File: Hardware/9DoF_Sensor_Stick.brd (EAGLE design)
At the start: 25.4 x 10.2 mm, 19 parts, among them U1 LSM9DS1

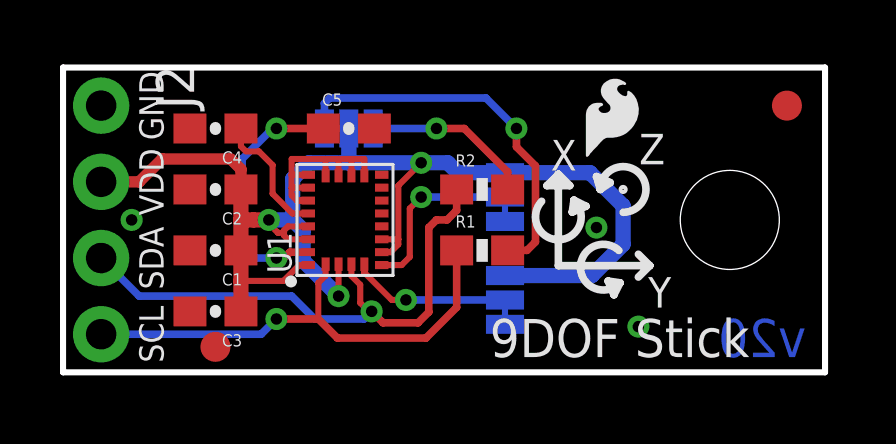
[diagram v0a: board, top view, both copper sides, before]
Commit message: Updating minor silk changes
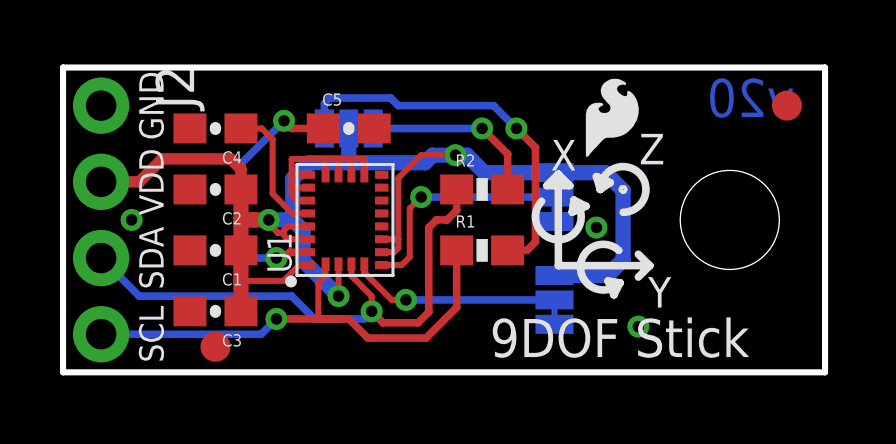
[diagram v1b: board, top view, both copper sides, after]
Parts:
- moved JP2 1.65 mm to (16.4, 2.41)
- moved JP3 1.65 mm to (16.4, 5.84)
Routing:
- net SDO_M: track 5.99 -> 7.64 mm
- net SDO_A/G: track 5.35 -> 7.00 mm
- net VDD: track 45.6 -> 46.2 mm
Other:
- board text added: "0x1C"
- board text added: "0x1E"
- board text added: "0x6A"
- board text added: "0x6B"
- board text removed: "0"
- board text removed: "1"

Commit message: QC Fixes
-Updated VDD trace width to 20mil throughout.
-Reduced overall length from 1.0" to 0.9".
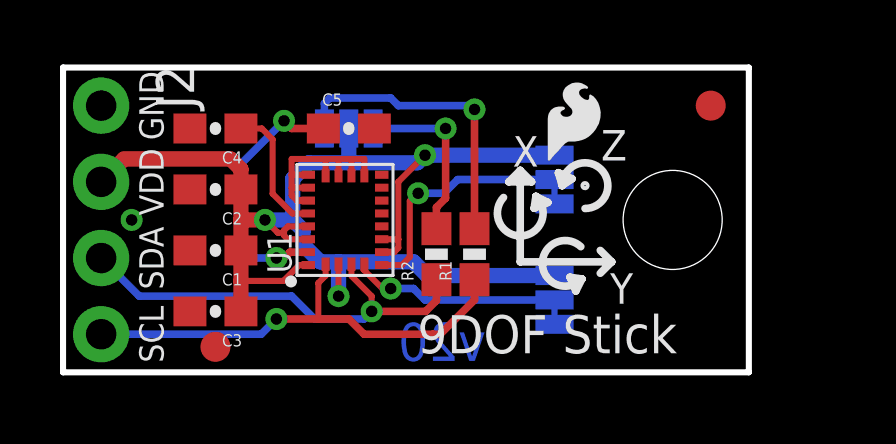
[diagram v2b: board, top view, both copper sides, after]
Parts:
- moved R2 2.64 mm to (12.4, 3.94), turned to 90 degrees
- moved FD1 2.54 mm to (21.6, 8.89)
- moved H1 1.91 mm to (20.3, 5.08)
- moved LOGO3 1.66 mm to (20.3, 8.51)
- moved LOGO1 1.28 mm to (15.9, 6.73)
- moved JP3 0.58 mm to (16.4, 6.43)
- moved R1 0.28 mm to (13.7, 3.94), turned to 90 degrees
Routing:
- net SDA: track 18.7 -> 14.8 mm
- net N$2: track 12.8 -> 10.1 mm
- net VDD: track 46.2 -> 44.9 mm
- net SCL: track 16.6 -> 15.9 mm
- net GND: vias 3 -> 1
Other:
- board size 25.4 x 10.2 mm -> 22.9 x 10.2 mm
- board text added: "ACC/ GYR"
- board text removed: "ACC/GYR"
